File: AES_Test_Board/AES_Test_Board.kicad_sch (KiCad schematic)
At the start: 34 parts, among them J1 Conn_02x06_Top_Bottom, J2 Conn_02x06_Top_Bottom, U3 TCR3RM10A

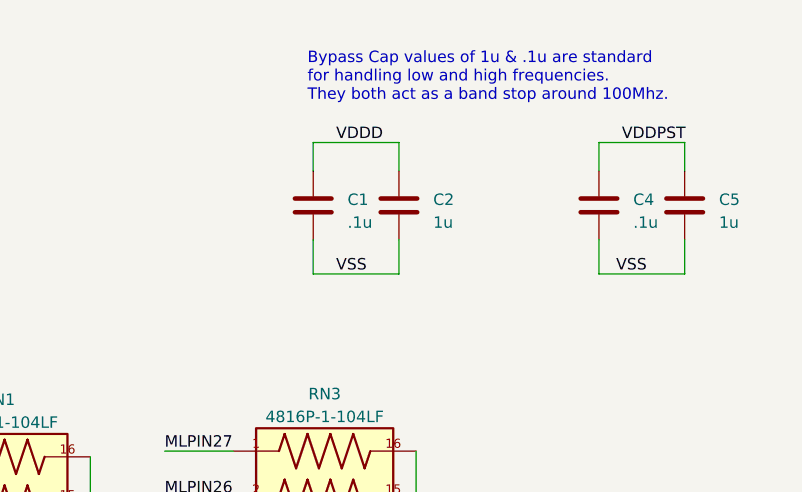
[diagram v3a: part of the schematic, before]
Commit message: Added 3 capacitors per power rail and changed pads to 0603
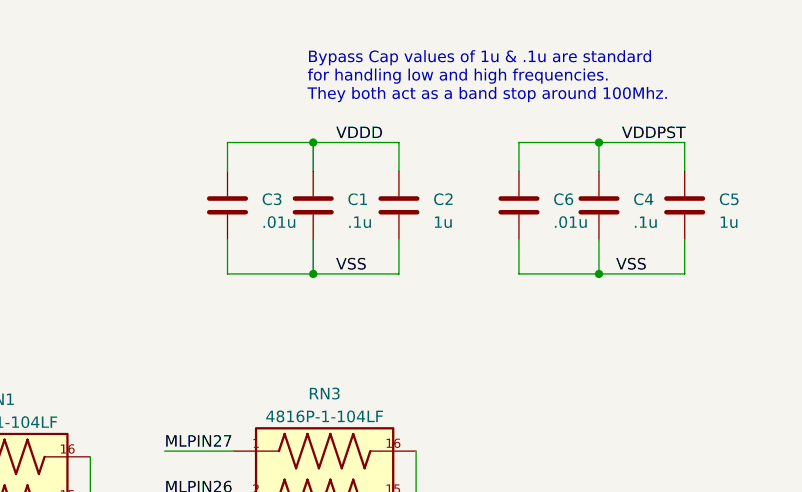
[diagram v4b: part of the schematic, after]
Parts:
- added C3, C6: .01u, Capacitor_SMD:C_0603_1608Metric_Pad1.08x0.95mm_HandSolder, symbol Device:C
- C1, C2, C4, C5, C7, C8: footprint Capacitor_SMD:C_0805_2012Metric_Pad1.18x1.45mm_HandSolder -> Capacitor_SMD:C_0603_1608Metric_Pad1.08x0.95mm_HandSolder
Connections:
- net VDDD: now also C3.1
- net VDDPST: now also C6.1
- net VSS: now also C3.2, C6.2
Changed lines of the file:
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@@
   (junction (at 208.28 132.08) (diameter 0) (color 0 0 0 0)
   )
+  (junction (at 233.045 26.035) (diameter 0) (color 0 0 0 0)
+  )
   (junction (at 208.28 76.2) (diameter 0) (color 0 0 0 0)
   )
@@
   (junction (at 244.475 137.16) (diameter 0) (color 0 0 0 0)
   )
+  (junction (at 264.795 40.64) (diameter 0) (color 0 0 0 0)
+  )
   (junction (at 208.28 127) (diameter 0) (color 0 0 0 0)
   )
   (junction (at 279.4 95.885) (diameter 0) (color 0 0 0 0)
   )
+  (junction (at 264.795 26.035) (diameter 0) (color 0 0 0 0)
+  )
   (junction (at 279.4 116.205) (diameter 0) (color 0 0 0 0)
+  )
+  (junction (at 233.045 40.64) (diameter 0) (color 0 0 0 0)
   )
   (junction (at 208.28 81.28) (diameter 0) (color 0 0 0 0)
@@
   (no_connect (at 48.26 76.2))
   (no_connect (at 48.26 73.66))
+  (wire (pts (xy 255.905 26.035) (xy 264.795 26.035))
+    (stroke (width 0) (type default))
+  )
   (wire (pts (xy 125.095 60.325) (xy 125.73 60.325))
     (stroke (width 0) (type default))
@@
     (stroke (width 0) (type default))
   )
+  (wire (pts (xy 223.52 40.64) (xy 233.045 40.64))
+    (stroke (width 0) (type default))
+  )
   (wire (pts (xy 165.1 55.245) (xy 175.895 55.245))
     (stroke (width 0) (type default))
@@
   )
   (wire (pts (xy 180.34 106.68) (xy 187.96 106.68))
+    (stroke (width 0) (type default))
+  )
+  (wire (pts (xy 223.52 26.035) (xy 233.045 26.035))
     (stroke (width 0) (type default))
   )
@@
     (stroke (width 0) (type default))
   )
+  (wire (pts (xy 255.905 40.64) (xy 264.795 40.64))
+    (stroke (width 0) (type default))
+  )
   (wire (pts (xy 165.1 62.865) (xy 175.895 62.865))
     (stroke (width 0) (type default))
@@
     (stroke (width 0) (type default))
   )
+  (wire (pts (xy 223.52 36.83) (xy 223.52 40.64))
+    (stroke (width 0) (type default))
+  )
   (wire (pts (xy 180.34 86.36) (xy 187.96 86.36))
     (stroke (width 0) (type default))
@@
   )
   (wire (pts (xy 165.1 75.565) (xy 175.895 75.565))
+    (stroke (width 0) (type default))
+  )
+  (wire (pts (xy 255.905 29.21) (xy 255.905 26.035))
     (stroke (width 0) (type default))
   )
@@
     (stroke (width 0) (type default))
   )
+  (wire (pts (xy 223.52 29.21) (xy 223.52 26.035))
+    (stroke (width 0) (type default))
+  )
   (wire (pts (xy 165.1 70.485) (xy 175.895 70.485))
     (stroke (width 0) (type default))
@@
   )
   (wire (pts (xy 274.32 26.035) (xy 274.32 29.21))
+    (stroke (width 0) (type default))
+  )
+  (wire (pts (xy 255.905 36.83) (xy 255.905 40.64))
     (stroke (width 0) (type default))
   )
@@
       (effects (font (size 1.27 1.27)) (justify left))
     )
-    (property "Footprint" "Capacitor_SMD:C_0805_2012Metric_Pad1.18x1.45mm_HandSolder" (at 265.7602 36.83 0)
+    (property "Footprint" "Capacitor_SMD:C_0603_1608Metric_Pad1.08x0.95mm_HandSolder" (at 265.7602 36.83 0)
       (effects (font (size 1.27 1.27)) hide)
     )
@@
       (effects (font (size 1.27 1.27)) (justify left))
     )
-    (property "Footprint" "Capacitor_SMD:C_0805_2012Metric_Pad1.18x1.45mm_HandSolder" (at 234.0102 36.83 0)
+    (property "Footprint" "Capacitor_SMD:C_0603_1608Metric_Pad1.08x0.95mm_HandSolder" (at 234.0102 36.83 0)
       (effects (font (size 1.27 1.27)) hide)
     )
@@
       (effects (font (size 1.27 1.27)) (justify left))
     )
-    (property "Footprint" "Capacitor_SMD:C_0805_2012Metric_Pad1.18x1.45mm_HandSolder" (at 67.0052 139.7 0)
+    (property "Footprint" "Capacitor_SMD:C_0603_1608Metric_Pad1.08x0.95mm_HandSolder" (at 67.0052 139.7 0)
       (effects (font (size 1.27 1.27)) hide)
     )
@@
         (path "/2678a414-2391-4aaa-b756-2ce84b941c0a"
           (reference "RSTN1") (unit 1)
+        )
+      )
+    )
+  )
+  (symbol (lib_id "Device:C") (at 255.905 33.02 0) (unit 1)
+    (in_bom yes) (on_board yes) (dnp no)
+    (property "Reference" "C6" (at 259.715 32.385 0)
+      (effects (font (size 1.27 1.27)) (justify left))
+    )
+    (property "Value" ".01u" (at 259.715 34.925 0)
+      (effects (font (size 1.27 1.27)) (justify left))
+    )
+    (property "Footprint" "Capacitor_SMD:C_0603_1608Metric_Pad1.08x0.95mm_HandSolder" (at 256.8702 36.83 0)
+      (effects (font (size 1.27 1.27)) hide)
+    )
+    (property "Datasheet" "~" (at 255.905 33.02 0)
+      (effects (font (size 1.27 1.27)) hide)
+    )
+    (pin "1")
+    (pin "2")
+    (instances
+      (project "AES_Test_Board"
+        (path "/2678a414-2391-4aaa-b756-2ce84b941c0a"
+          (reference "C6") (unit 1)
         )
       )
@@
     )
   )
+  (symbol (lib_id "Device:C") (at 223.52 33.02 0) (unit 1)
+    (in_bom yes) (on_board yes) (dnp no)
+    (property "Reference" "C3" (at 227.33 32.385 0)
+      (effects (font (size 1.27 1.27)) (justify left))
+    )
+    (property "Value" ".01u" (at 227.33 34.925 0)
+      (effects (font (size 1.27 1.27)) (justify left))
+    )
+    (property "Footprint" "Capacitor_SMD:C_0603_1608Metric_Pad1.08x0.95mm_HandSolder" (at 224.4852 36.83 0)
+      (effects (font (size 1.27 1.27)) hide)
+    )
+    (property "Datasheet" "~" (at 223.52 33.02 0)
+      (effects (font (size 1.27 1.27)) hide)
+    )
+    (pin "1")
+    (pin "2")
+    (instances
+      (project "AES_Test_Board"
+        (path "/2678a414-2391-4aaa-b756-2ce84b941c0a"
+          (reference "C3") (unit 1)
+        )
+      )
+    )
+  )
   (symbol (lib_id "Connector_Generic:Conn_02x06_Top_Bottom") (at 53.34 71.12 0) (unit 1)
     (in_bom yes) (on_board yes) (dnp no)
@@
       (effects (font (size 1.27 1.27)) (justify left))
     )
-    (property "Footprint" "Capacitor_SMD:C_0805_2012Metric_Pad1.18x1.45mm_HandSolder" (at 275.2852 36.83 0)
+    (property "Footprint" "Capacitor_SMD:C_0603_1608Metric_Pad1.08x0.95mm_HandSolder" (at 275.2852 36.83 0)
       (effects (font (size 1.27 1.27)) hide)
     )
@@
       (effects (font (size 1.27 1.27)) (justify left))
     )
-    (property "Footprint" "Capacitor_SMD:C_0805_2012Metric_Pad1.18x1.45mm_HandSolder" (at 243.5352 36.83 0)
+    (property "Footprint" "Capacitor_SMD:C_0603_1608Metric_Pad1.08x0.95mm_HandSolder" (at 243.5352 36.83 0)
       (effects (font (size 1.27 1.27)) hide)
     )
@@
       (effects (font (size 1.27 1.27)) (justify left))
     )
-    (property "Footprint" "Capacitor_SMD:C_0805_2012Metric_Pad1.18x1.45mm_HandSolder" (at 40.3352 140.97 0)
-      (effects (font (size 1.27 1.27)) hide)
-    )
+    (property "Footprint" "Capacitor_SMD:C_0603_1608Metric_Pad1.08x0.95mm_HandSolder" (at 40.3352 140.97 0)
+      (effects (font (size 1.27 1.27)) hide)
+    )

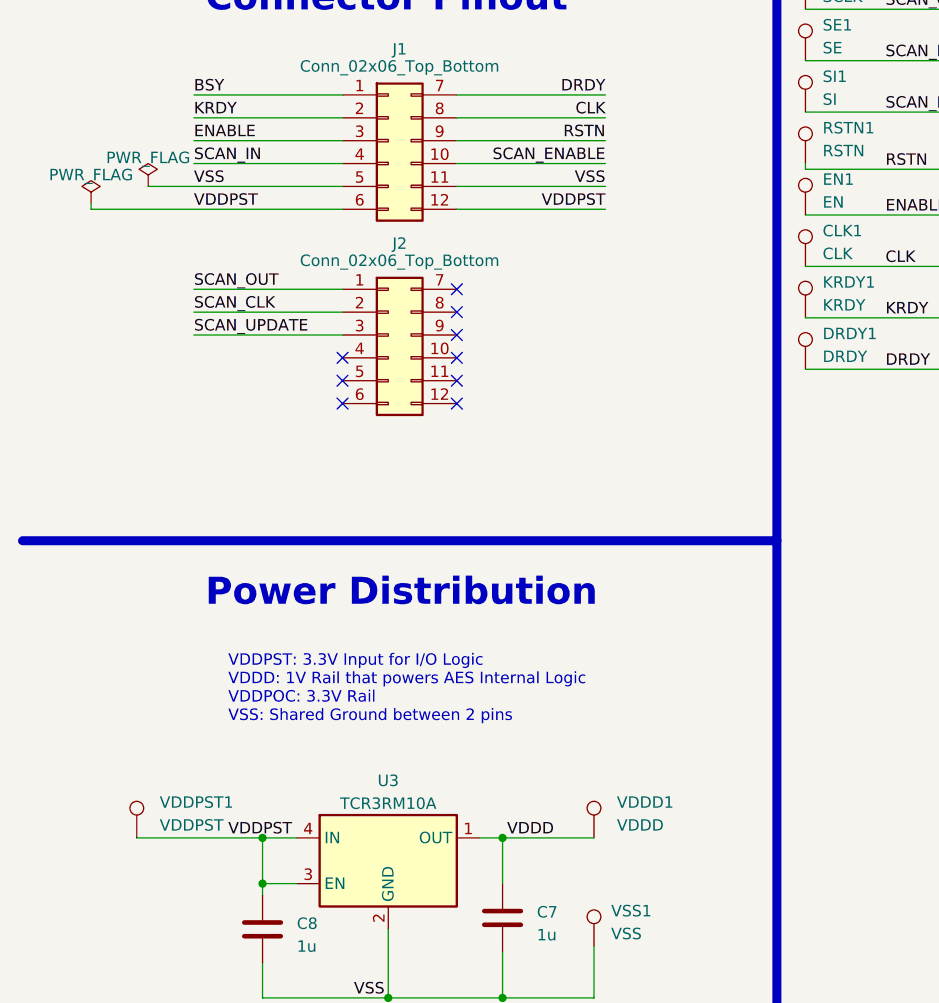
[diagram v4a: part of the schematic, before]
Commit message: Added Power measurement circuitry and regenerated gerbers
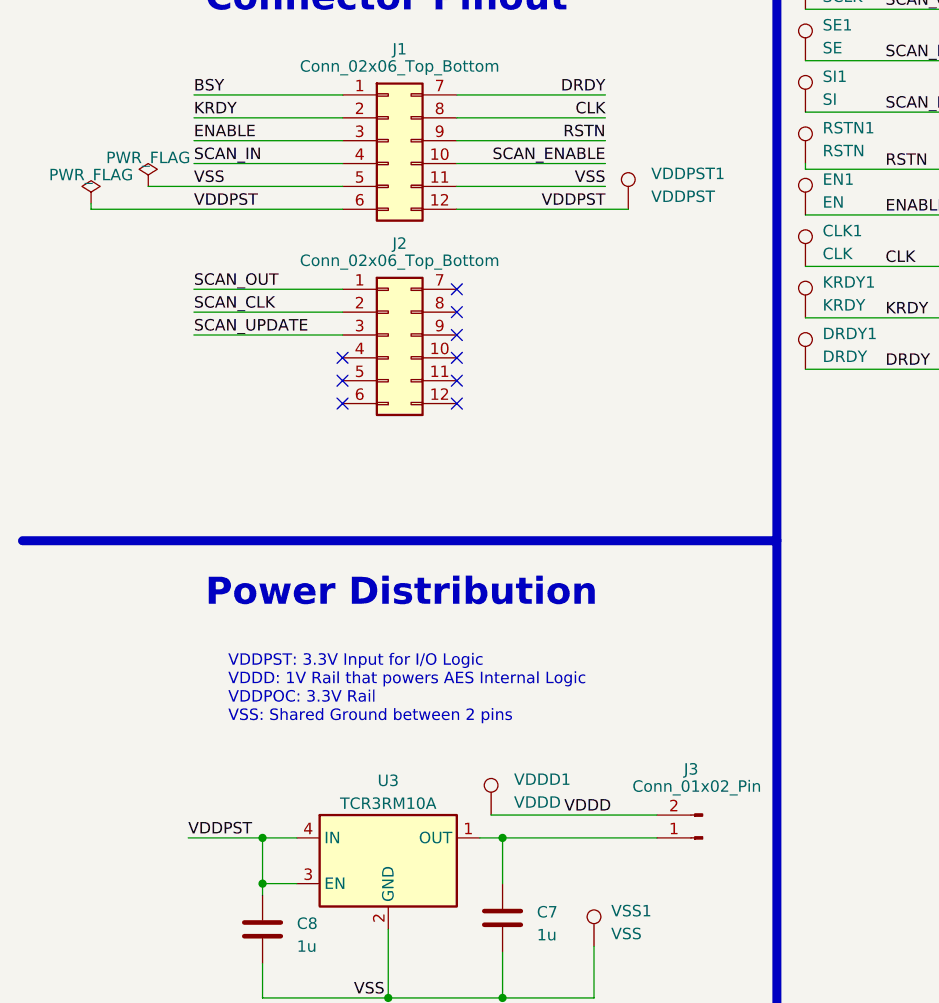
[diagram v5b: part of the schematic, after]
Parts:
- added J3: Conn_01x02_Pin, Connector_PinSocket_2.54mm:PinSocket_1x02_P2.54mm_Vertical, symbol Connector:Conn_01x02_Pin
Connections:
- net VDDD: now also J3.2 (Pin_2); no longer C7.1, U3.1 (OUT)
- new net: C7.1, J3.1 (Pin_1), U3.1 (OUT)
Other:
- moved on the sheet: VDDD1, VDDPST1
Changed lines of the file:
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@@
 (kicad_sch (version 20230121) (generator eeschema)
   (paper "A4")
+  (junction (at 208.28 142.24) (diameter 0) (color 0 0 0 0)
+  )
+  (junction (at 208.28 137.16) (diameter 0) (color 0 0 0 0)
+  )
+  (junction (at 244.475 80.645) (diameter 0) (color 0 0 0 0)
+  )
+  (junction (at 279.4 106.045) (diameter 0) (color 0 0 0 0)
+  )
+  (junction (at 244.475 142.24) (diameter 0) (color 0 0 0 0)
+  )
+  (junction (at 279.4 121.285) (diameter 0) (color 0 0 0 0)
+  )
+  (junction (at 39.37 132.08) (diameter 0) (color 0 0 0 0)
+  )
+  (junction (at 208.28 132.08) (diameter 0) (color 0 0 0 0)
+  )
+  (junction (at 233.045 26.035) (diameter 0) (color 0 0 0 0)
+  )
+  (junction (at 208.28 76.2) (diameter 0) (color 0 0 0 0)
+  )
+  (junction (at 208.28 71.12) (diameter 0) (color 0 0 0 0)
+  )
+  (junction (at 244.475 65.405) (diameter 0) (color 0 0 0 0)
+  )
+  (junction (at 244.475 121.92) (diameter 0) (color 0 0 0 0)
+  )
+  (junction (at 244.475 90.805) (diameter 0) (color 0 0 0 0)
+  )
+  (junction (at 244.475 75.565) (diameter 0) (color 0 0 0 0)
+  )
+  (junction (at 244.475 132.08) (diameter 0) (color 0 0 0 0)
+  )
+  (junction (at 208.28 121.92) (diameter 0) (color 0 0 0 0)
+  )
+  (junction (at 208.28 66.04) (diameter 0) (color 0 0 0 0)
+  )
+  (junction (at 244.475 95.885) (diameter 0) (color 0 0 0 0)
+  )
+  (junction (at 244.475 111.76) (diameter 0) (color 0 0 0 0)
+  )
+  (junction (at 279.4 90.805) (diameter 0) (color 0 0 0 0)
+  )
+  (junction (at 208.28 111.76) (diameter 0) (color 0 0 0 0)
+  )
+  (junction (at 244.475 116.84) (diameter 0) (color 0 0 0 0)
+  )
+  (junction (at 208.28 96.52) (diameter 0) (color 0 0 0 0)
+  )
+  (junction (at 244.475 85.725) (diameter 0) (color 0 0 0 0)
+  )
+  (junction (at 279.4 100.965) (diameter 0) (color 0 0 0 0)
+  )
+  (junction (at 279.4 111.125) (diameter 0) (color 0 0 0 0)
+  )
   (junction (at 39.37 127) (diameter 0) (color 0 0 0 0)
-  )
-  (junction (at 208.28 142.24) (diameter 0) (color 0 0 0 0)
-  )
-  (junction (at 208.28 137.16) (diameter 0) (color 0 0 0 0)
-  )
-  (junction (at 244.475 80.645) (diameter 0) (color 0 0 0 0)
-  )
-  (junction (at 279.4 106.045) (diameter 0) (color 0 0 0 0)
-  )
-  (junction (at 244.475 142.24) (diameter 0) (color 0 0 0 0)
-  )
-  (junction (at 279.4 121.285) (diameter 0) (color 0 0 0 0)
-  )
-  (junction (at 39.37 132.08) (diameter 0) (color 0 0 0 0)
-  )
-  (junction (at 208.28 132.08) (diameter 0) (color 0 0 0 0)
-  )
-  (junction (at 233.045 26.035) (diameter 0) (color 0 0 0 0)
-  )
-  (junction (at 208.28 76.2) (diameter 0) (color 0 0 0 0)
-  )
-  (junction (at 208.28 71.12) (diameter 0) (color 0 0 0 0)
-  )
-  (junction (at 244.475 65.405) (diameter 0) (color 0 0 0 0)
-  )
-  (junction (at 244.475 121.92) (diameter 0) (color 0 0 0 0)
-  )
-  (junction (at 244.475 90.805) (diameter 0) (color 0 0 0 0)
-  )
-  (junction (at 244.475 75.565) (diameter 0) (color 0 0 0 0)
-  )
-  (junction (at 244.475 132.08) (diameter 0) (color 0 0 0 0)
-  )
-  (junction (at 208.28 121.92) (diameter 0) (color 0 0 0 0)
-  )
-  (junction (at 208.28 66.04) (diameter 0) (color 0 0 0 0)
-  )
-  (junction (at 244.475 95.885) (diameter 0) (color 0 0 0 0)
-  )
-  (junction (at 244.475 111.76) (diameter 0) (color 0 0 0 0)
-  )
-  (junction (at 279.4 90.805) (diameter 0) (color 0 0 0 0)
-  )
-  (junction (at 208.28 111.76) (diameter 0) (color 0 0 0 0)
-  )
-  (junction (at 244.475 116.84) (diameter 0) (color 0 0 0 0)
-  )
-  (junction (at 208.28 96.52) (diameter 0) (color 0 0 0 0)
-  )
-  (junction (at 244.475 85.725) (diameter 0) (color 0 0 0 0)
-  )
-  (junction (at 279.4 100.965) (diameter 0) (color 0 0 0 0)
-  )
-  (junction (at 279.4 111.125) (diameter 0) (color 0 0 0 0)
   )
   (junction (at 208.28 91.44) (diameter 0) (color 0 0 0 0)
@@
     (stroke (width 0) (type default))
   )
-  (wire (pts (xy 66.04 127) (xy 76.2 127))
+  (wire (pts (xy 66.04 127) (xy 83.185 127))
     (stroke (width 0) (type default))
   )
@@
   )
   (wire (pts (xy 233.045 26.035) (xy 233.045 29.21))
-    (stroke (width 0) (type default))
-  )
-  (wire (pts (xy 25.4 127) (xy 39.37 127))
     (stroke (width 0) (type default))
   )
@@
     (stroke (width 0) (type default))
   )
+  (wire (pts (xy 31.115 127) (xy 39.37 127))
+    (stroke (width 0) (type default))
+  )
   (wire (pts (xy 180.34 111.76) (xy 187.96 111.76))
     (stroke (width 0) (type default))
@@
     (stroke (width 0) (type default))
   )
-  (wire (pts (xy 60.96 57.15) (xy 77.47 57.15))
+  (wire (pts (xy 60.96 57.15) (xy 80.01 57.15))
     (stroke (width 0) (type default))
   )
@@
     (stroke (width 0) (type default))
   )
+  (wire (pts (xy 64.77 124.46) (xy 83.185 124.46))
+    (stroke (width 0) (type default))
+  )
   (wire (pts (xy 165.1 83.185) (xy 175.895 83.185))
     (stroke (width 0) (type default))
@@
     (effects (font (size 1.27 1.27)) (justify left bottom))
   )
-  (label "VDDPST" (at 35.56 127 0) (fields_autoplaced)
-    (effects (font (size 1.27 1.27)) (justify left bottom))
-  )
   (label "CLK" (at 108.585 63.5 0) (fields_autoplaced)
     (effects (font (size 1.27 1.27)) (justify left bottom))
@@
     (effects (font (size 1.27 1.27)) (justify left bottom))
   )
+  (label "VDDPST" (at 31.115 127 0) (fields_autoplaced)
+    (effects (font (size 1.27 1.27)) (justify left bottom))
+  )
   (label "MLPIN22" (at 175.895 95.885 180) (fields_autoplaced)
     (effects (font (size 1.27 1.27)) (justify right bottom))
@@
     (effects (font (size 1.27 1.27)) (justify left bottom))
   )
-  (label "VDDD" (at 71.755 127 180) (fields_autoplaced)
+  (label "VDDD" (at 78.105 124.46 180) (fields_autoplaced)
     (effects (font (size 1.27 1.27)) (justify right bottom))
   )
@@
     )
   )
-  (symbol (lib_id "Connector:TestPoint") (at 25.4 127 0) (unit 1)
-    (in_bom yes) (on_board yes) (dnp no) (fields_autoplaced)
-    (property "Reference" "VDDPST1" (at 27.94 123.063 0)
-      (effects (font (size 1.27 1.27)) (justify left))
-    )
-    (property "Value" "VDDPST" (at 27.94 125.603 0)
-      (effects (font (size 1.27 1.27)) (justify left))
-    )
-    (property "Footprint" "TestPoint:TestPoint_Keystone_5000-5004_Miniature" (at 30.48 127 0)
-      (effects (font (size 1.27 1.27)) hide)
-    )
-    (property "Datasheet" "~" (at 30.48 127 0)
+  (symbol (lib_id "Connector:TestPoint") (at 80.01 57.15 0) (unit 1)
+    (in_bom yes) (on_board yes) (dnp no) (fields_autoplaced)
+    (property "Reference" "VDDPST1" (at 82.55 53.213 0)
+      (effects (font (size 1.27 1.27)) (justify left))
+    )
+    (property "Value" "VDDPST" (at 82.55 55.753 0)
+      (effects (font (size 1.27 1.27)) (justify left))
+    )
+    (property "Footprint" "TestPoint:TestPoint_Keystone_5000-5004_Miniature" (at 85.09 57.15 0)
+      (effects (font (size 1.27 1.27)) hide)
+    )
+    (property "Datasheet" "~" (at 85.09 57.15 0)
       (effects (font (size 1.27 1.27)) hide)
     )
@@
     )
   )
-  (symbol (lib_id "Connector:TestPoint") (at 76.2 127 0) (unit 1)
-    (in_bom yes) (on_board yes) (dnp no) (fields_autoplaced)
-    (property "Reference" "VDDD1" (at 78.74 123.063 0)
-      (effects (font (size 1.27 1.27)) (justify left))
-    )
-    (property "Value" "VDDD" (at 78.74 125.603 0)
-      (effects (font (size 1.27 1.27)) (justify left))
-    )
-    (property "Footprint" "TestPoint:TestPoint_Keystone_5000-5004_Miniature" (at 81.28 127 0)
-      (effects (font (size 1.27 1.27)) hide)
-    )
-    (property "Datasheet" "~" (at 81.28 127 0)
+  (symbol (lib_id "Connector:TestPoint") (at 64.77 124.46 0) (unit 1)
+    (in_bom yes) (on_board yes) (dnp no) (fields_autoplaced)
+    (property "Reference" "VDDD1" (at 67.31 120.523 0)
+      (effects (font (size 1.27 1.27)) (justify left))
+    )
+    (property "Value" "VDDD" (at 67.31 123.063 0)
+      (effects (font (size 1.27 1.27)) (justify left))
+    )
+    (property "Footprint" "TestPoint:TestPoint_Keystone_5000-5004_Miniature" (at 69.85 124.46 0)
+      (effects (font (size 1.27 1.27)) hide)
+    )
+    (property "Datasheet" "~" (at 69.85 124.46 0)
       (effects (font (size 1.27 1.27)) hide)
     )
@@
         )
       )
+    )
+  )
+  (symbol (lib_id "Connector:Conn_01x02_Pin") (at 88.265 127 180) (unit 1)
+    (in_bom yes) (on_board yes) (dnp no)
+    (property "Reference" "J3" (at 86.995 119.38 0)
+      (effects (font (size 1.27 1.27)))
+    )
+    (property "Value" "Conn_01x02_Pin" (at 87.63 121.285 0)
+      (effects (font (size 1.27 1.27)))
+    )
+    (property "Footprint" "Connector_PinSocket_2.54mm:PinSocket_1x02_P2.54mm_Vertical" (at 88.265 127 0)
+      (effects (font (size 1.27 1.27)) hide)
+    )
+    (property "Datasheet" "~" (at 88.265 127 0)
+      (effects (font (size 1.27 1.27)) hide)
+    )
+    (pin "1")
+    (pin "2")
+    (instances
+      (project "AES_Test_Board"
+        (path "/2678a414-2391-4aaa-b756-2ce84b941c0a"
+          (reference "J3") (unit 1)
+        )
+      )
